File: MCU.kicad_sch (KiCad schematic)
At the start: 24 parts, among them J2 USB_C_Receptacle_USB2.0_16P, J8 FTSH-105-01-L-DV-K-A, U1 STM32G0B1CBTx, Y1 Crystal_GND24

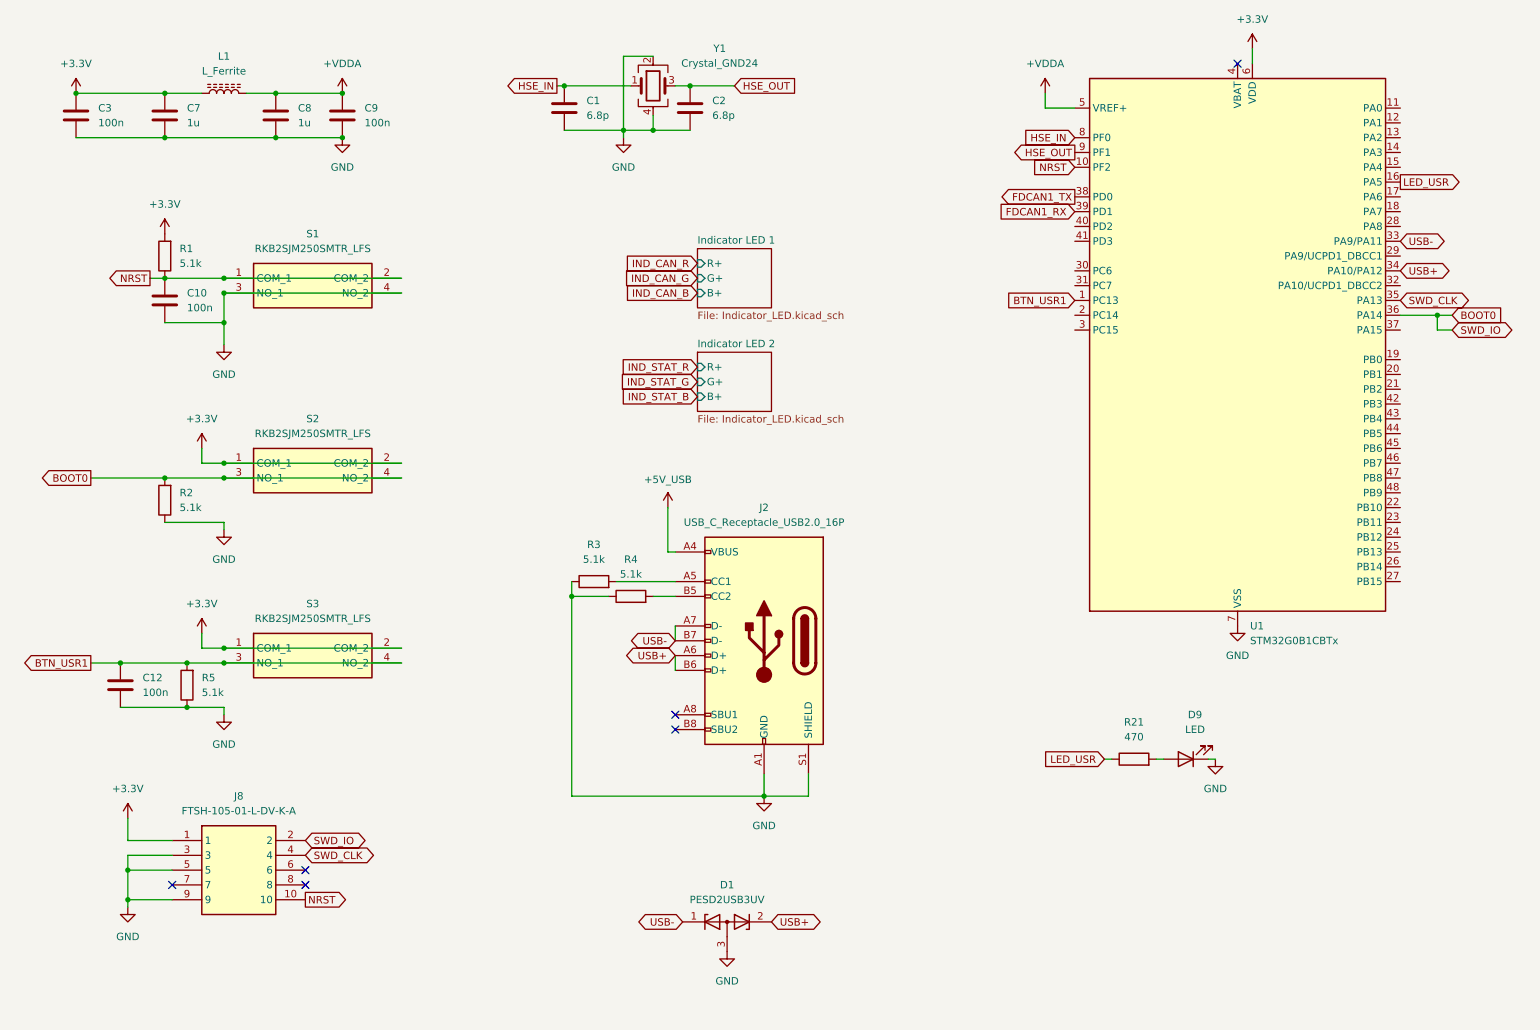
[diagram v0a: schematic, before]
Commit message: updated pinout, begin layout
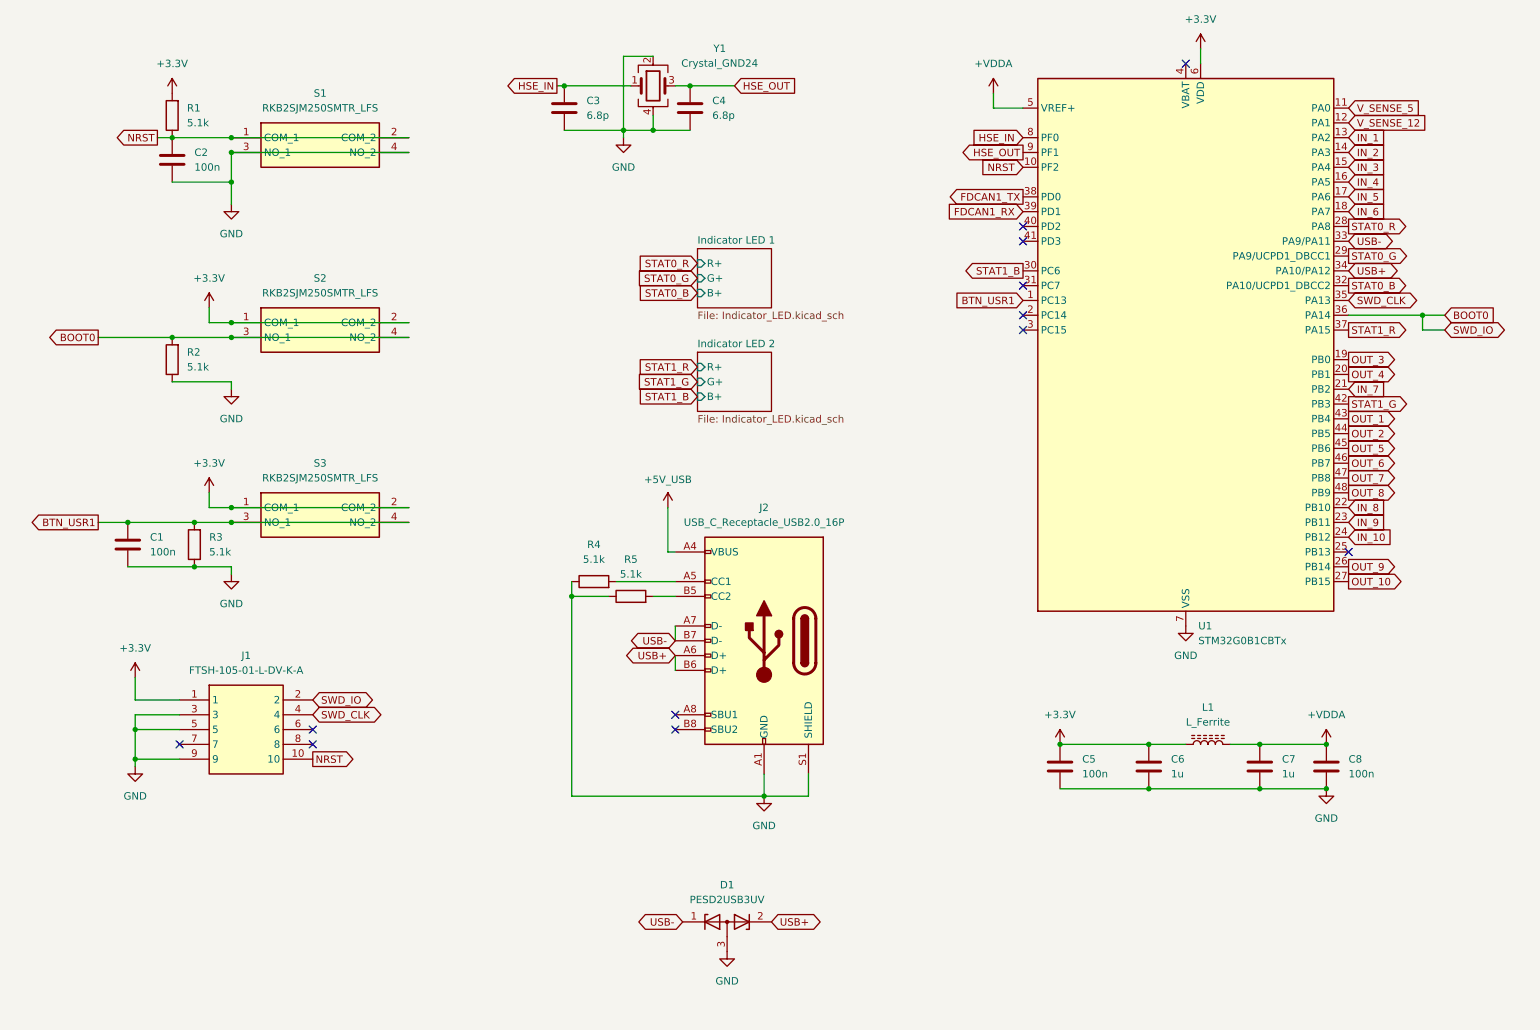
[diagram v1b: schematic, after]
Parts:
- removed D9: LED, LED_SMD:LED_0603_1608Metric_Pad1.05x0.95mm_HandSolder, symbol Device:LED
- removed R21: 470, Resistor_SMD:R_0603_1608Metric_Pad0.98x0.95mm_HandSolder, symbol Device:R
- renumbered C12 to C1, C10 to C2, C1 to C3, C2 to C4, C3 to C5, C7 to C6, C8 to C7, C9 to C8, J8 to J1, R5 to R3, R3 to R4, R4 to R5
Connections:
- net V_SENSE_5: now reaches U1.11 (PA0)
- net V_SENSE_12: now reaches U1.12 (PA1)
- net IN_1: now reaches U1.13 (PA2)
- net IN_2: now reaches U1.14 (PA3)
- net IN_3: now reaches U1.15 (PA4)
- net IN_5: now reaches U1.17 (PA6)
- net IN_6: now reaches U1.18 (PA7)
- net OUT_3: now reaches U1.19 (PB0)
- net OUT_4: now reaches U1.20 (PB1)
- net IN_7: now reaches U1.21 (PB2)
- net IN_8: now reaches U1.22 (PB10)
- net IN_9: now reaches U1.23 (PB11)
- net IN_10: now reaches U1.24 (PB12)
- net OUT_9: now reaches U1.26 (PB14)
- net OUT_10: now reaches U1.27 (PB15)
- net STAT0_R: now reaches U1.28 (PA8)
- net STAT0_G: now reaches U1.29 (PA9/UCPD1_DBCC1)
- net STAT1_B: now reaches U1.30 (PC6)
- net STAT0_B: now reaches U1.32 (PA10/UCPD1_DBCC2)
- net STAT1_R: now reaches U1.37 (PA15)
- net STAT1_G: now reaches U1.42 (PB3)
- net OUT_1: now reaches U1.43 (PB4)
- net OUT_2: now reaches U1.44 (PB5)
- net OUT_5: now reaches U1.45 (PB6)
- net OUT_6: now reaches U1.46 (PB7)
- net OUT_7: now reaches U1.47 (PB8)
- net OUT_8: now reaches U1.48 (PB9)
- net LED_USR renamed IN_4
- no-connect marks 6 -> 12
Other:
- moved on the sheet: C1, C2, C5, C6, C7, C8, J1, L1, R1, R2, R3, S1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

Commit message: more work on layout
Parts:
- removed C8: 100n, Capacitor_SMD:C_0603_1608Metric_Pad1.08x0.95mm_HandSolder, symbol Device:C
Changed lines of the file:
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@@
-	)
-	(junction
-		(at 247.65 149.86)
-		(diameter 0)
-		(color 0 0 0 0)
 	)
 	(junction
 		(at 264.16 68.58)
-		(diameter 0)
-		(color 0 0 0 0)
-	)
-	(junction
-		(at 247.65 142.24)
 		(diameter 0)
 		(color 0 0 0 0)
@@
 					(unit 1)
 				)
-			)
-		)
-	)
-	(symbol
-		(lib_id "Device:C")
-		(at 247.65 146.05 0)
-		(unit 1)
-		(body_style 1)
-		(exclude_from_sim no)
-		(in_bom yes)
-		(on_board yes)
-		(in_pos_files yes)
-		(dnp no)
-		(fields_autoplaced yes)
-		(property "Reference" "C8"
-			(at 251.46 144.7799 0)
-			(show_name no)
-			(do_not_autoplace no)
-			(effects
-				(font
-					(size 1.27 1.27)
-				)
-				(justify left)
-			)
-		)
-		(property "Value" "100n"
-			(at 251.46 147.3199 0)
-			(show_name no)
-			(do_not_autoplace no)
-			(effects
-				(font
-					(size 1.27 1.27)
-				)
-				(justify left)
-			)
-		)
-		(property "Footprint" "Capacitor_SMD:C_0603_1608Metric_Pad1.08x0.95mm_HandSolder"
-			(at 248.6152 149.86 0)
-			(hide yes)
-			(show_name no)
-			(do_not_autoplace no)
-			(effects
-				(font
-					(size 1.27 1.27)
-				)
-			)
-		)
-		(property "Datasheet" ""
-			(at 247.65 146.05 0)
-			(hide yes)
-			(show_name no)
-			(do_not_autoplace no)
-			(effects
-				(font
-					(size 1.27 1.27)
-				)
-			)
-		)
-		(property "Description" "Unpolarized capacitor"
-			(at 247.65 146.05 0)
-			(hide yes)
-			(show_name no)
-			(do_not_autoplace no)
-			(effects
-				(font
-					(size 1.27 1.27)
-				)
-			)
-		)
-		(pin "1"
-		)
-		(pin "2"
-		)
-		(instances
-			(project "RSC-LV3-SwitchSense"
-				(path "/ea09e839-df61-4c3f-abdc-aa7ae2f772fe/4aa7ee16-37d7-4a92-b053-2235cd7f2d7b"
-					(reference "C8")
-					(unit 1)
-				)

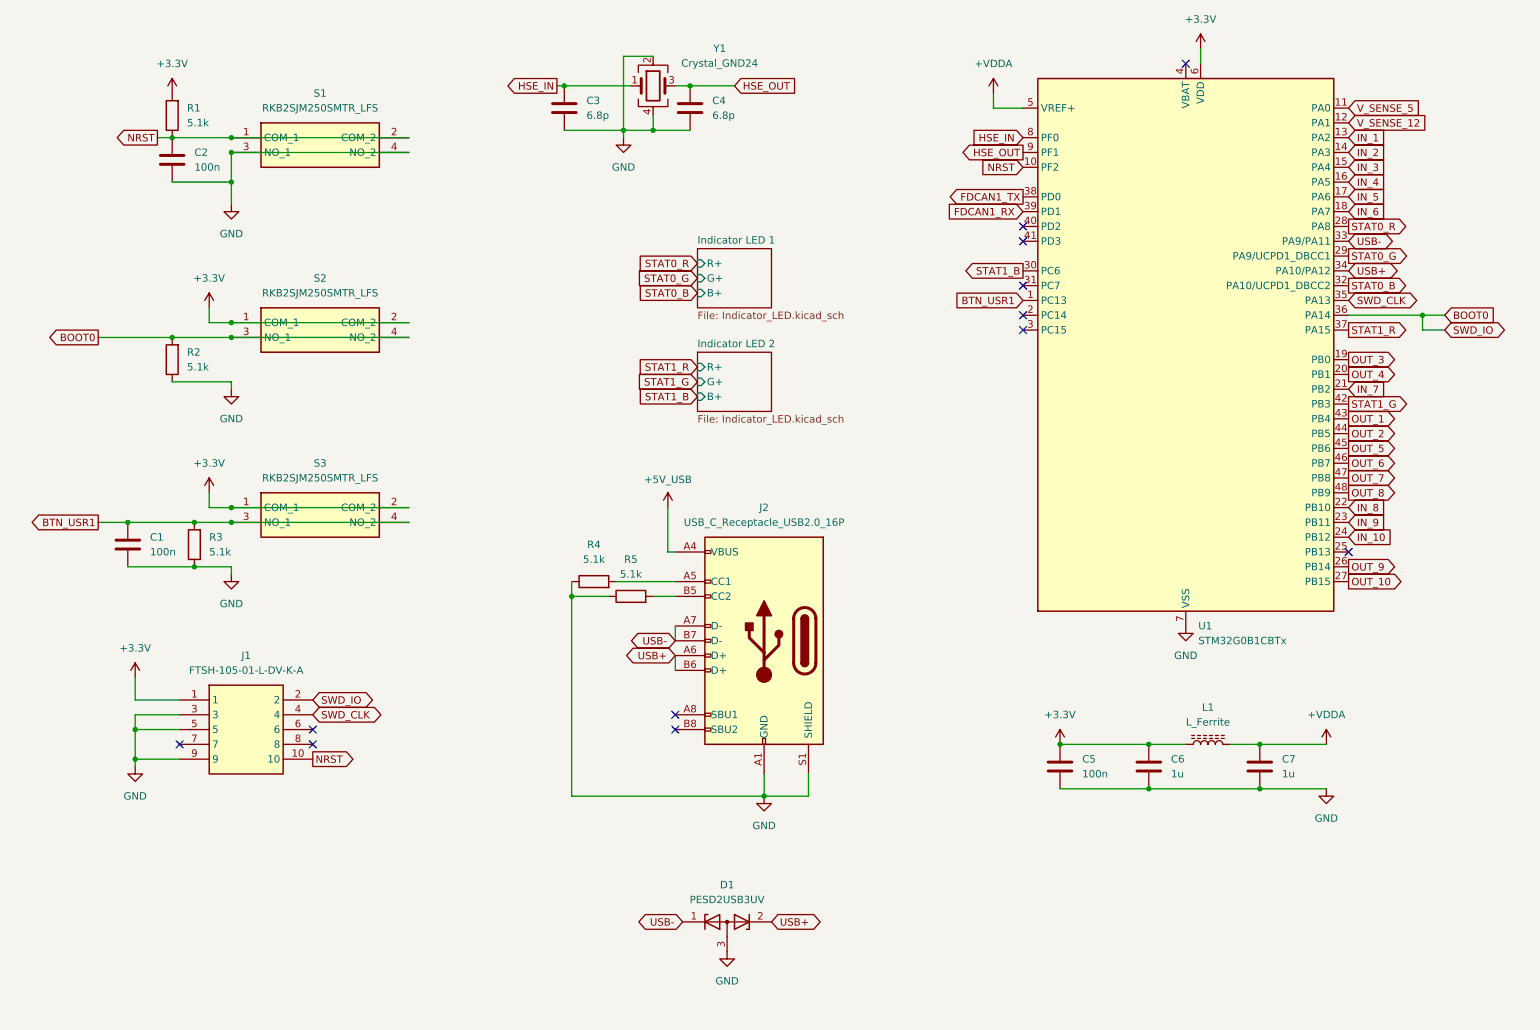
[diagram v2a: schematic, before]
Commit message: add second CAN and backup domain components
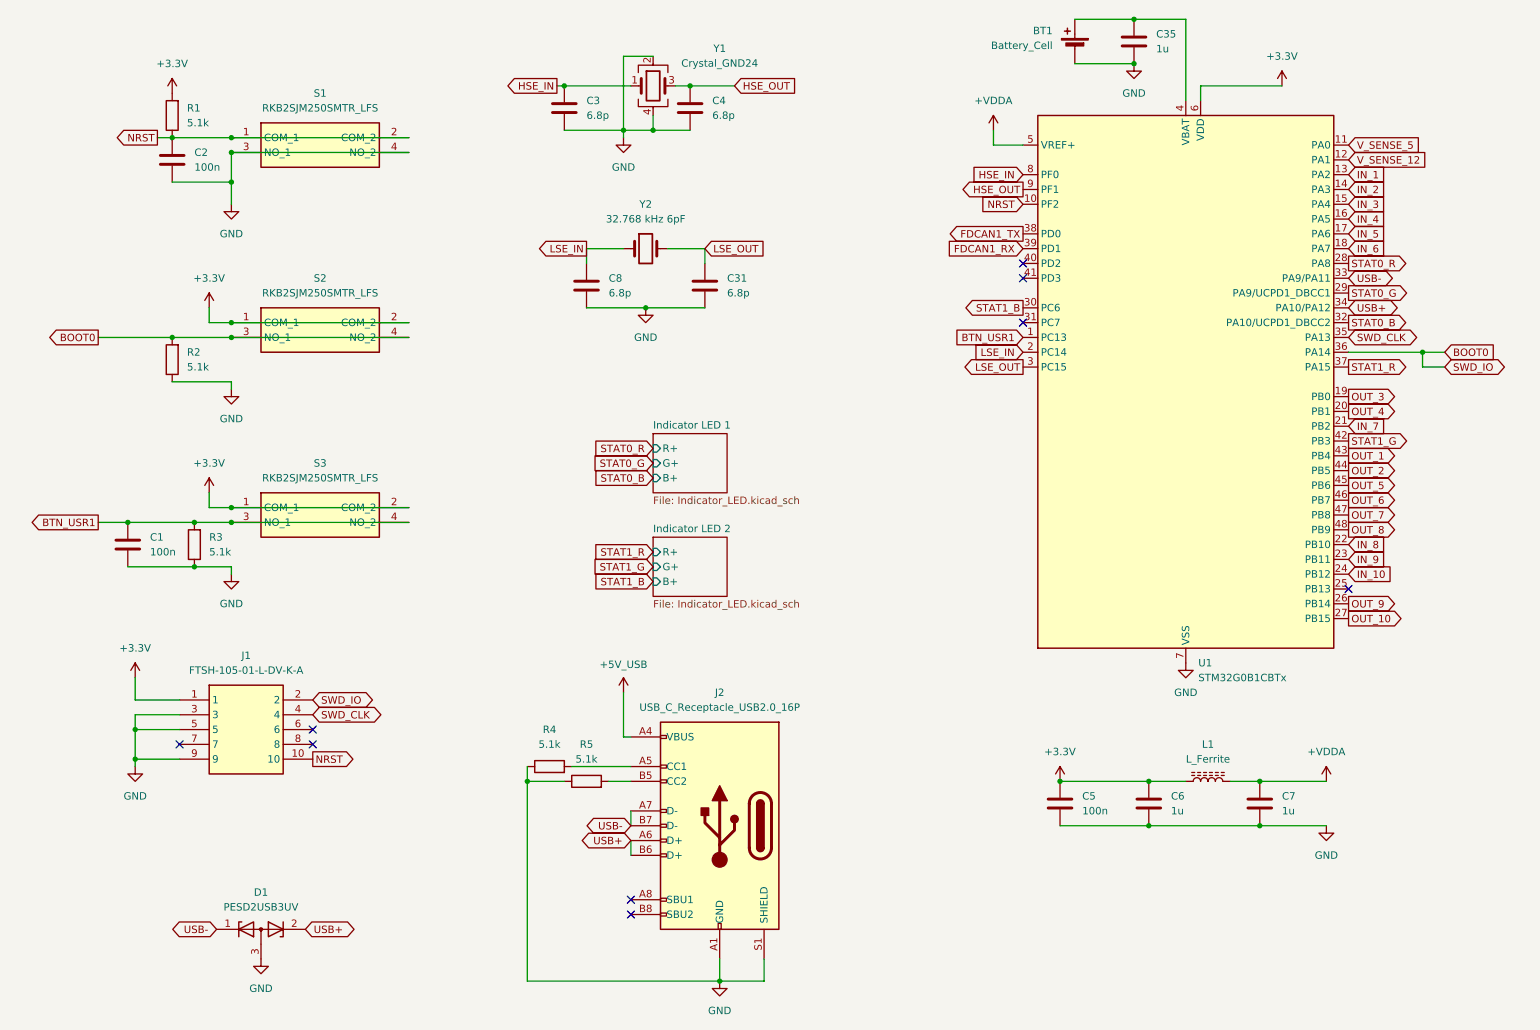
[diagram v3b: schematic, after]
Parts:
- added BT1: Battery_Cell, symbol Device:Battery_Cell
- added C31, C8: 6.8p, Capacitor_SMD:C_0603_1608Metric_Pad1.08x0.95mm_HandSolder, symbol Device:C
- added C35: 1u, Capacitor_SMD:C_0603_1608Metric_Pad1.08x0.95mm_HandSolder, symbol Device:C
- added Y2: 32.768 kHz 6pF, Crystal:Crystal_C26-LF_D2.1mm_L6.5mm_Horizontal, symbol Device:Crystal
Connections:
- net GND: now also BT1.2 (-), C31.2, C35.2, C8.2
- net LSE_IN: now reaches U1.2 (PC14)
- net LSE_IN: now also C8.1, Y2.1
- net LSE_OUT: now reaches U1.3 (PC15)
- net LSE_OUT: now also C31.1, Y2.2
- net at U1.4 (VBAT): now also BT1.1 (+), C35.1
- no-connect marks 12 -> 9
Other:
- moved on the sheet: C5, C6, C7, D1, J2, L1, R4, R5, U1
